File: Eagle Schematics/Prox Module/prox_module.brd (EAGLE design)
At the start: 64.4 x 80 mm, 52 parts, among them IC1 74LS14N, IC2 74LS14N, Q1 16MHZ

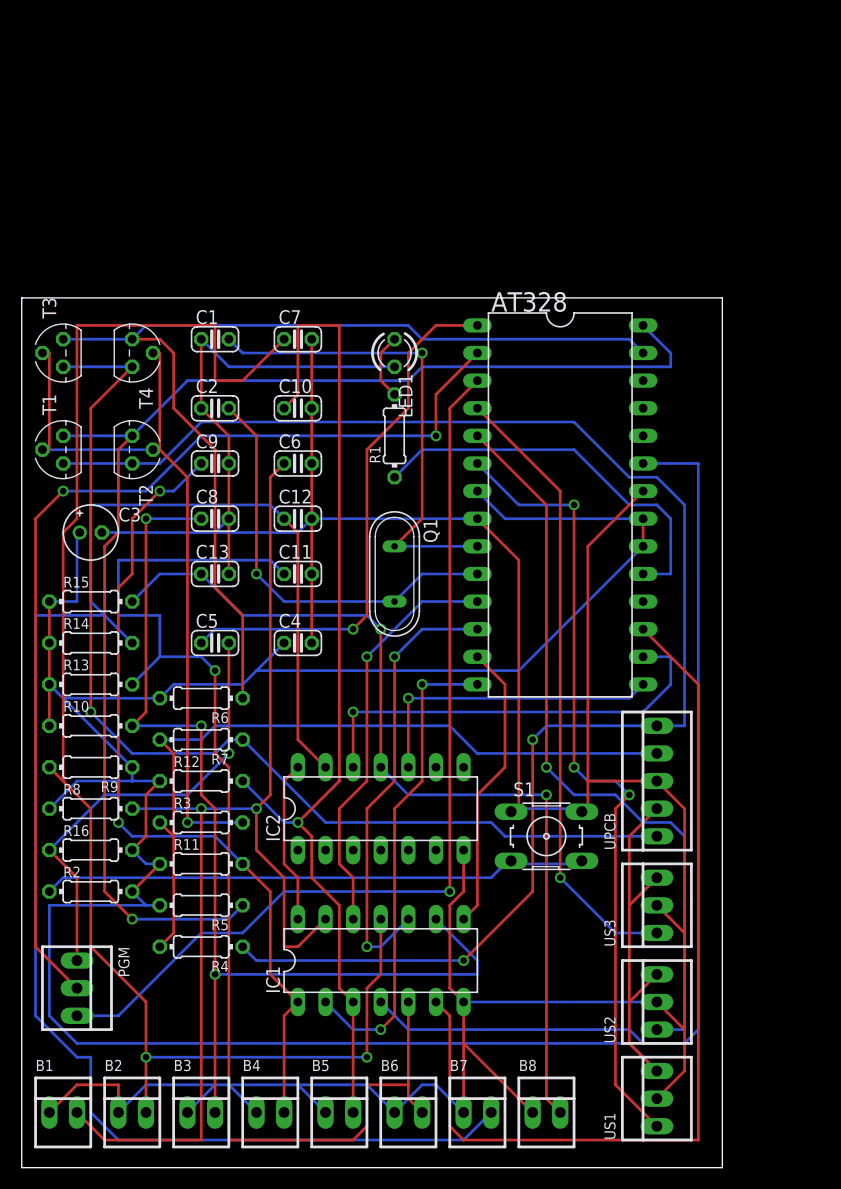
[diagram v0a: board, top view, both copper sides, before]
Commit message: Modified prox design, added BOM
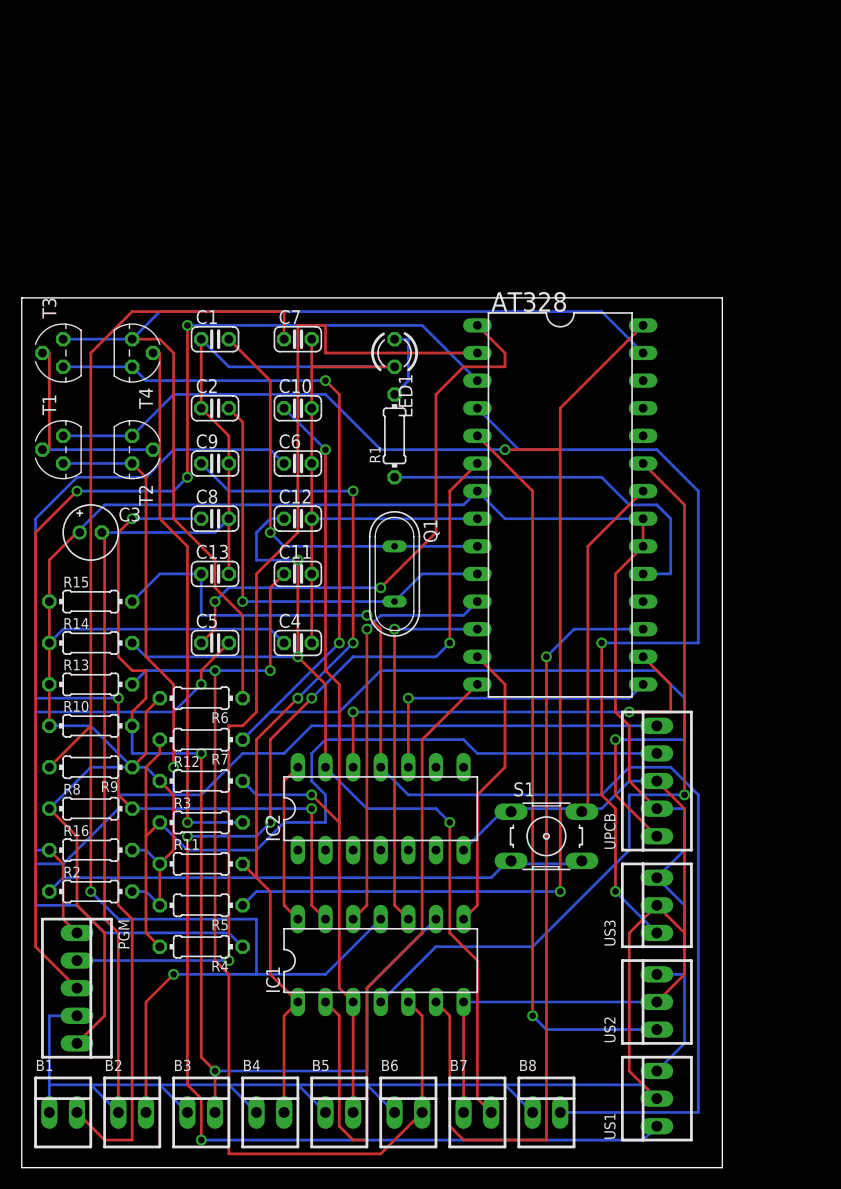
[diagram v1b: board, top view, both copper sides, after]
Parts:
- PGM: value 22-23-2031 -> 22-23-2051; device con-molex:22-23-2031 -> con-molex:22-23-2051
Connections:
- net 5V: now also PGM.5
- net GND: now also PGM.4
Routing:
- net BMP-DBNCE7: track 150.9 -> 87.1 mm, vias 0 -> 3
- net US1DATA: track 73.3 -> 124.4 mm, vias 3 -> 5
- net GND: track 327.3 -> 374.4 mm
- net BMP-DBNCE8: track 84.7 -> 115.2 mm, vias 2 -> 1
- net SDA: track 97.5 -> 123.2 mm, vias 1 -> 3
- net 5V: track 253.0 -> 230.6 mm
- net BMP-DBNCE1: track 105.8 -> 126.4 mm
- net US3DATA: track 57.3 -> 75.1 mm, vias 1 -> 2
- net BMP-OUT8: track 88.5 -> 70.9 mm, vias 0 -> 1
- net BMP-DBNCE5: track 94.7 -> 77.9 mm, vias 1 -> 2
- net BMP-OUT4: track 44.5 -> 61.1 mm, vias 2 -> 0
- net RX-TX: track 87.1 -> 102.3 mm, vias 1 -> 3
- net BMP-DBNCE6: track 112.9 -> 97.7 mm, vias 1 -> 2
- net SCL: track 140.5 -> 126.0 mm, vias 2 -> 1
- net SCL-5V: track 120.6 -> 134.4 mm, vias 1 -> 2
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
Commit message: Made final V1.4 revisions
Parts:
- removed AT328: (no value), ic-package:DIL28-6
- added ATMEGA: 328, ic-package:DIL28-6
- added C14: 100uF, rcl:E2-5
- added C15: 0.1uF, rcl:C025-024X044
- T1, T2, T3, T4: value (none) -> BJT
- moved B7 6.35 mm to (47.0, 8.89)
- moved B8 6.35 mm to (53.3, 8.89)
- moved S1 6.35 mm to (53.3, 34.3)
- moved C10 6.35 mm to (30.5, 73.7)
- moved C11 6.35 mm to (30.5, 58.4)
- moved C12 6.35 mm to (30.5, 63.5)
- moved C4 6.35 mm to (30.5, 52.1)
- moved C6 6.35 mm to (30.5, 68.6)
- moved C7 6.35 mm to (30.5, 80.0)
- moved B4 6.35 mm to (27.9, 8.89)
- moved R10 6.35 mm to (11.4, 44.5)
- moved R14 6.35 mm to (11.4, 52.1)
- moved R15 6.35 mm to (11.4, 55.9)
- moved R16 6.35 mm to (11.4, 33.0)
- moved R2 6.35 mm to (11.4, 29.2)
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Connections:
- removed net VCC: IC1.14, IC2.14
- net 3V: now also C14.+, C15.1
- net 5V: now also ATMEGA.20, ATMEGA.21, ATMEGA.7, IC1.14, IC2.14; no longer AT328.20, AT328.21, AT328.7
- net BMP-OUT1: now also ATMEGA.11; no longer AT328.11
- net BMP-OUT2: now also ATMEGA.12; no longer AT328.12
- net BMP-OUT3: now also ATMEGA.13; no longer AT328.13
- net BMP-OUT4: now also ATMEGA.14; no longer AT328.14
- net BMP-OUT5: now also ATMEGA.15; no longer AT328.15
- net BMP-OUT6: now also ATMEGA.16; no longer AT328.16
- net BMP-OUT7: now also ATMEGA.17; no longer AT328.17
- net BMP-OUT8: now also ATMEGA.23; no longer AT328.23
- net CLK-1: now also ATMEGA.9; no longer AT328.9
- net CLK-2: now also ATMEGA.10; no longer AT328.10
- net GND: now also ATMEGA.22, ATMEGA.8, C14.-, C15.2; no longer AT328.22, AT328.8
- net LEDNET-1: now also ATMEGA.19; no longer AT328.19
- net RST-2: now also ATMEGA.1; no longer AT328.1
- net RX-TX: now also ATMEGA.3; no longer AT328.3
- net SCL-5V: now also ATMEGA.28; no longer AT328.28
- net SDA-5V: now also ATMEGA.27; no longer AT328.27
- net TX-RX: now also ATMEGA.2; no longer AT328.2
- net US1DATA: now also ATMEGA.6; no longer AT328.6
- net US2DATA: now also ATMEGA.5; no longer AT328.5
- net US3DATA: now also ATMEGA.4; no longer AT328.4
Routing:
- net 5V: track 230.6 -> 273.3 mm
- net US1DATA: track 124.4 -> 84.7 mm, vias 5 -> 0
- net BMP-DBNCE4: track 79.8 -> 116.4 mm, vias 3 -> 0
- net US3DATA: track 75.1 -> 111.0 mm, vias 2 -> 0
- net SDA: track 123.2 -> 88.9 mm, vias 3 -> 1
- net BMP-DBNCE2: track 133.1 -> 159.4 mm
- net SCL: track 126.0 -> 101.2 mm, vias 1 -> 2
- net BMP-DBNCE8: track 115.2 -> 91.2 mm, vias 1 -> 2
- net 3V: track 78.9 -> 98.4 mm, vias 0 -> 1
- net BMP-DBNCE5: track 77.9 -> 95.9 mm, vias 2 -> 1
- net BMP-DBNCE6: track 97.7 -> 114.3 mm, vias 2 -> 0
- net VCC: track 15.0 -> 0.00 mm
- net RST-SW: track 50.2 -> 61.4 mm
- net TX-RX: track 94.8 -> 105.9 mm, vias 1 -> 2
- net US2DATA: track 67.4 -> 77.6 mm, vias 1 -> 0
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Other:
- board size 64.4 x 80 mm -> 73.3 x 87.6 mm

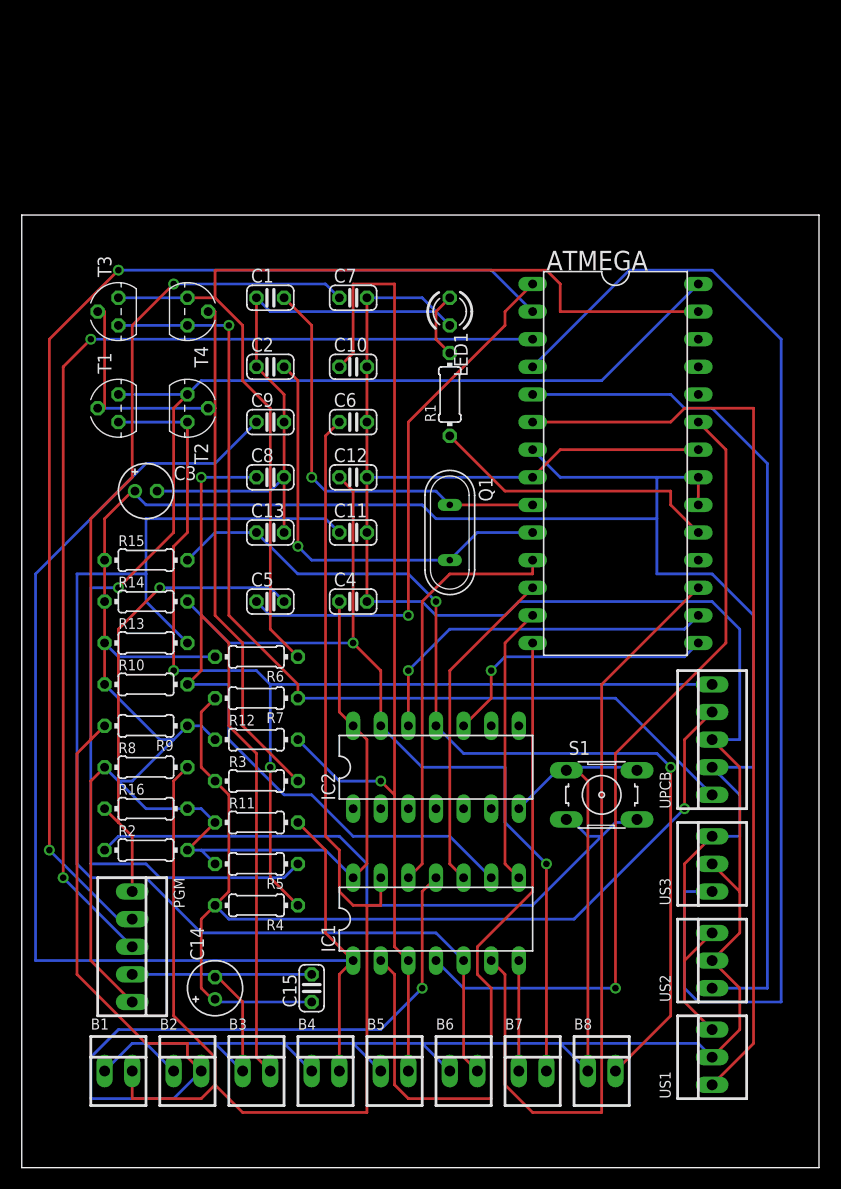
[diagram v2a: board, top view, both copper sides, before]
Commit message: Modified all schematics
Added a self debugging system.
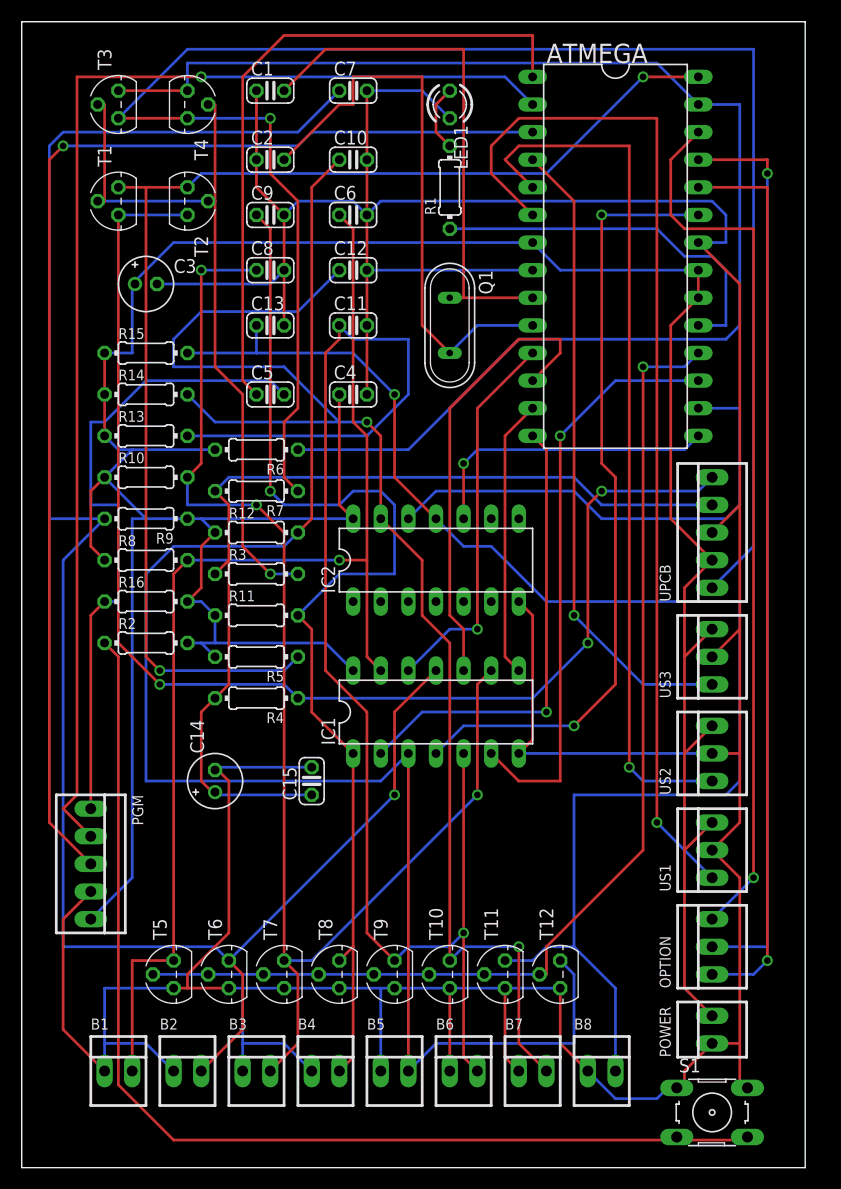
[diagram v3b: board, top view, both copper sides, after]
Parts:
- added OPTION: 22-23-2031, con-molex:22-23-2031
- added POWER: 22-23-2021, con-molex:22-23-2021
- added T10, T11, T12, T5, T6, T7, T8, T9: BJT, transistor:TO92-E1
- moved S1 30.9 mm to (63.5, 5.08)
- moved LED1 19.1 mm to (39.4, 97.8)
- moved T1 19.1 mm to (8.89, 88.9)
- moved T2 19.1 mm to (15.2, 88.9)
- moved T3 19.1 mm to (8.89, 97.8)
- moved T4 19.1 mm to (15.2, 97.8)
- moved C3 19.1 mm to (11.4, 81.3)
- moved C4 19.1 mm to (30.5, 71.1)
- moved C5 19.1 mm to (22.9, 71.1)
- moved IC2 19.1 mm to (38.1, 55.9)
- moved R12 19.1 mm to (21.6, 58.4)
- moved R13 19.1 mm to (11.4, 67.3)
- moved R14 19.1 mm to (11.4, 71.1)
- moved R15 19.1 mm to (11.4, 74.9)
- moved R6 19.1 mm to (21.6, 66.0)
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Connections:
- removed net BMP-DBNCE1: B1.2, C6.1, IC1.13, R8.2
- removed net BMP-DBNCE2: B2.2, C7.1, IC1.11, R9.2
- removed net BMP-DBNCE3: B3.2, C8.1, IC1.9, R10.2
- removed net BMP-DBNCE4: B4.2, C9.1, IC1.1, R11.2
- removed net BMP-DBNCE5: B5.2, C10.1, IC1.3, R12.2
- removed net BMP-DBNCE6: B6.2, C11.1, IC1.5, R13.2
- removed net BMP-DBNCE7: B7.2, C12.1, IC2.13, R14.2
- removed net BMP-DBNCE8: B8.2, C13.1, IC2.11, R15.2
- new net BMP-IN1: B1.2, C6.1, IC1.13, R8.2, T5.3
- new net BMP-IN2: B2.2, C7.1, IC1.11, R9.2, T6.3
- new net BMP-IN3: B3.2, C8.1, IC1.9, R10.2, T7.3
- new net BMP-IN4: B4.2, C9.1, IC1.1, R11.2, T8.3
- new net BMP-IN5: B5.2, C10.1, IC1.3, R12.2, T12.3
- new net BMP-IN6: B6.2, C11.1, IC1.5, R13.2, T9.3
- new net BMP-IN7: B7.2, C12.1, IC2.13, R14.2, T10.3
- new net BMP-IN8: B8.2, C13.1, IC2.11, R15.2, T11.3
- new net OPTION1: ATMEGA.24, OPTION.1
- new net OPTION2: ATMEGA.25, OPTION.2
- new net OPTION3: ATMEGA.26, OPTION.3
- new net TEST: ATMEGA.18, T10.2, T11.2, T12.2, T5.2, T6.2, T7.2, T8.2, T9.2
- net 5V: now also POWER.2
- net GND: now also POWER.1, T10.1, T11.1, T12.1, T5.1, T6.1, T7.1, T8.1, T9.1
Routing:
- net BMP-IN2: track 0.00 -> 171.7 mm, vias 0 -> 1
- net BMP-DBNCE2: track 159.4 -> 0.00 mm, vias 2 -> 0
- net BMP-IN5: track 0.00 -> 149.3 mm
- net BMP-IN8: track 0.00 -> 133.4 mm, vias 0 -> 1
- net BMP-IN6: track 0.00 -> 132.6 mm, vias 0 -> 1
- net BMP-IN7: track 0.00 -> 127.4 mm, vias 0 -> 2
- net BMP-DBNCE1: track 127.2 -> 0.00 mm
- net BMP-IN3: track 0.00 -> 124.3 mm, vias 0 -> 3
- net BMP-DBNCE4: track 116.4 -> 0.00 mm
- net BMP-DBNCE6: track 114.3 -> 0.00 mm
- net BMP-IN1: track 0.00 -> 111.3 mm, vias 0 -> 1
- net BMP-DBNCE3: track 107.5 -> 0.00 mm, vias 1 -> 0
- net BMP-IN4: track 0.00 -> 102.1 mm, vias 0 -> 1
- net TEST: track 0.00 -> 101.4 mm, vias 0 -> 1
- net BMP-DBNCE5: track 95.9 -> 0.00 mm, vias 1 -> 0
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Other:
- board size 73.3 x 87.6 mm -> 72.1 x 105.4 mm
